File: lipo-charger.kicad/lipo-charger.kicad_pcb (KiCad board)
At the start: 2 copper layers, 23 x 35 mm, 20 parts, among them J1 JST-PH2 Device, J2 Alt Device, J3 JST-PH2 Bat, J4 Alt Bat, U1 MCP73831-2-OT, U2 XB6166IS

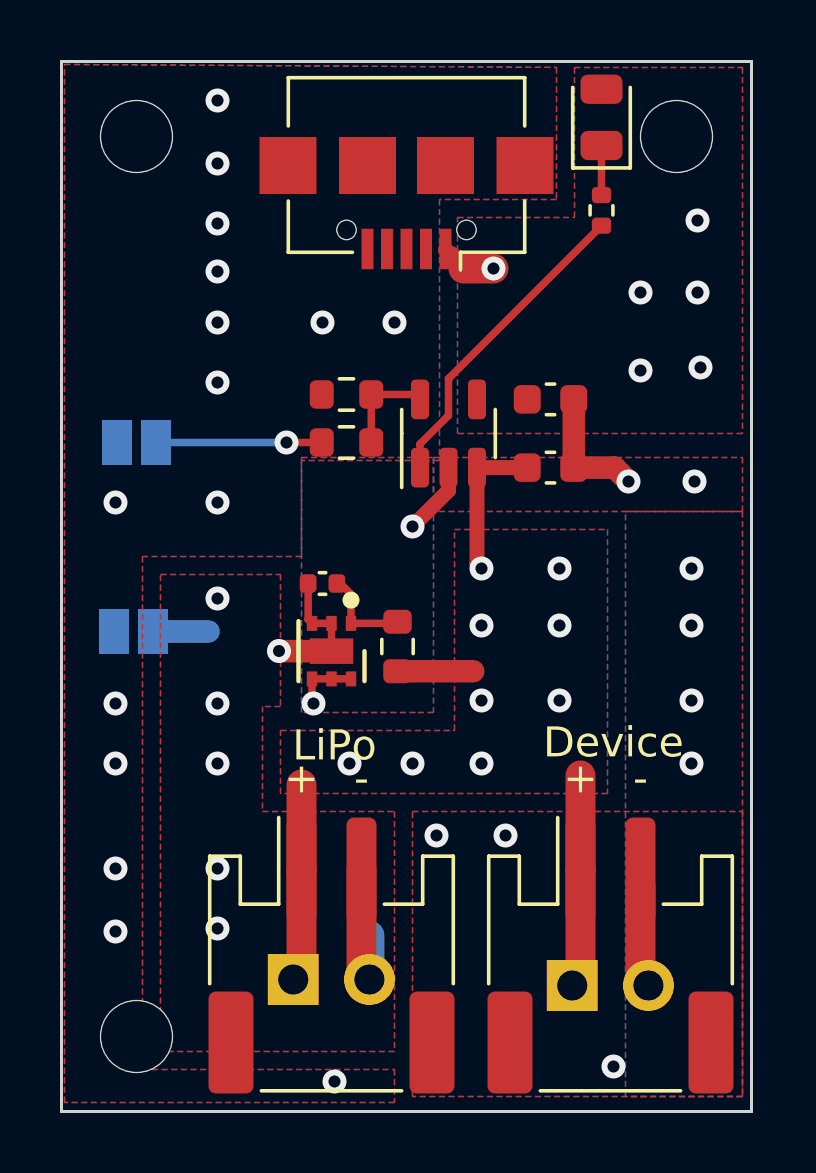
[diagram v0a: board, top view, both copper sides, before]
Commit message: Rev 0.91: remove alternative connectors for LiPo and device
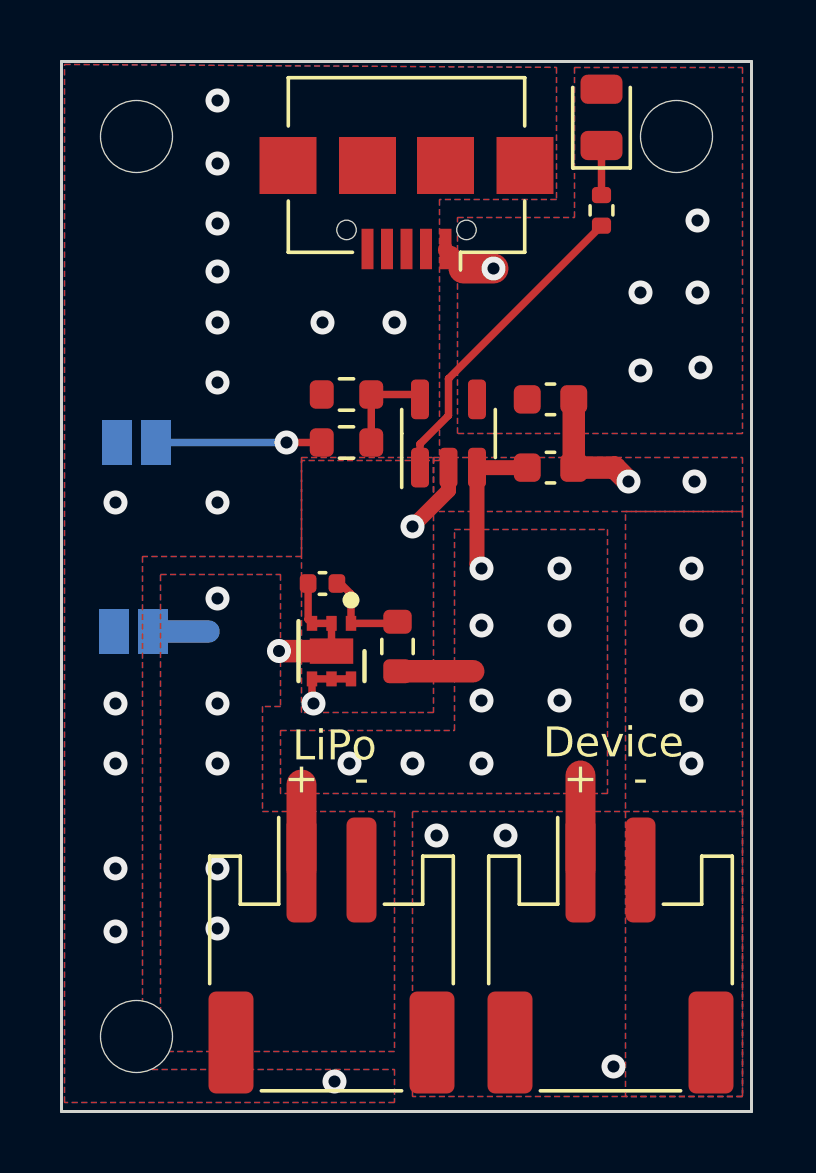
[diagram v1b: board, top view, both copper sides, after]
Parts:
- removed J2: Alt Device, Connector_PinHeader_2.54mm:PinHeader_1x02_P2.54mm_Vertical
- removed J4: Alt Bat, Connector_PinHeader_2.54mm:PinHeader_1x02_P2.54mm_Vertical
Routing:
- net +BATT: track 21.4 -> 13.6 mm
- net -BATT: track 11.8 -> 6.56 mm
- net GND: track 12.7 -> 9.27 mm
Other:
- board text added: "https://github.com/bablokb/ pcb-lipo-charger Rev: 0.91"
- board text removed: "https://github.com/bablokb/ pcb-lipo-charger Rev: 0.9"
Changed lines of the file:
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@@
     (pad "" np_thru_hole circle (at 0 0) (size 2.4 2.4) (drill 2.4) (layers F&B.Cu *.Mask))
-  )
-  (footprint "Connector_PinHeader_2.54mm:PinHeader_1x02_P2.54mm_Vertical" (layer "B.Cu")
-    (at 117.025 130.8 -90)
-    (descr "Through hole straight pin header, 1x02, 2.54mm pitch, single row")
-    (tags "Through hole pin header THT 1x02 2.54mm single row")
-    (property "Sheetfile" "lipo-charger.kicad_sch")
-    (property "Sheetname" "")
-    (property "exclude_from_bom" "")
-    (attr through_hole exclude_from_bom)
-    (fp_text reference "J2" (at -2.1 -1.275 180) (layer "B.SilkS") hide
-      (effects (font (size 1 1) (thickness 0.15)) (justify mirror))
-    )
-    (fp_text value "Alt Device" (at 0 -4.87 90) (layer "B.Fab") hide
-      (effects (font (size 1 1) (thickness 0.15)) (justify mirror))
-    )
-    (fp_text user "${REFERENCE}" (at 0 -1.27) (layer "B.Fab")
-      (effects (font (size 1 1) (thickness 0.15)) (justify mirror))
-    )
-    (fp_line (start 1.33 -1.27) (end 1.33 -3.87) (layer "B.SilkS") (width 0.12))
-    (fp_line (start -1.33 1.33) (end 0 1.33) (layer "B.SilkS") (width 0.12))
-    (fp_line (start -1.33 -1.27) (end 1.33 -1.27) (layer "B.SilkS") (width 0.12))
-    (fp_line (start -1.33 -3.87) (end 1.33 -3.87) (layer "B.SilkS") (width 0.12))
-    (fp_line (start -1.33 -1.27) (end -1.33 -3.87) (layer "B.SilkS") (width 0.12))
-    (fp_line (start -1.33 0) (end -1.33 1.33) (layer "B.SilkS") (width 0.12))
-    (fp_line (start -1.8 -4.35) (end 1.8 -4.35) (layer "B.CrtYd") (width 0.05))
-    (fp_line (start 1.8 1.8) (end -1.8 1.8) (layer "B.CrtYd") (width 0.05))
-    (fp_line (start -1.8 1.8) (end -1.8 -4.35) (layer "B.CrtYd") (width 0.05))
-    (fp_line (start 1.8 -4.35) (end 1.8 1.8) (layer "B.CrtYd") (width 0.05))
-    (fp_line (start 1.27 1.27) (end 1.27 -3.81) (layer "B.Fab") (width 0.1))
-    (fp_line (start -0.635 1.27) (end 1.27 1.27) (layer "B.Fab") (width 0.1))
-    (fp_line (start -1.27 -3.81) (end -1.27 0.635) (layer "B.Fab") (width 0.1))
-    (fp_line (start -1.27 0.635) (end -0.635 1.27) (layer "B.Fab") (width 0.1))
-    (fp_line (start 1.27 -3.81) (end -1.27 -3.81) (layer "B.Fab") (width 0.1))
-    (pad "1" thru_hole rect (at 0 0 270) (size 1.7 1.7) (drill 1) (layers *.Cu *.Mask)
-      (net 3 "+BATT") (pinfunction "Pin_1") (pintype "passive"))
-    (pad "2" thru_hole oval (at 0 -2.54 270) (size 1.7 1.7) (drill 1) (layers *.Cu *.Mask)
-      (net 2 "GND") (pinfunction "Pin_2") (pintype "passive"))
-    (model "${KICAD6_3DMODEL_DIR}/Connector_PinHeader_2.54mm.3dshapes/PinHeader_1x02_P2.54mm_Vertical.wrl"
-      (offset (xyz 0 0 0))
-      (scale (xyz 1 1 1))
-      (rotate (xyz 0 0 0))
-    )
-  )
-  (footprint "Connector_PinHeader_2.54mm:PinHeader_1x02_P2.54mm_Vertical" (layer "B.Cu")
-    (at 107.725 130.6 -90)
-    (descr "Through hole straight pin header, 1x02, 2.54mm pitch, single row")
-    (tags "Through hole pin header THT 1x02 2.54mm single row")
-    (property "Sheetfile" "lipo-charger.kicad_sch")
-    (property "Sheetname" "")
-    (property "exclude_from_bom" "")
-    (attr through_hole exclude_from_bom)
-    (fp_text reference "J4" (at -2.05 -1.125 180) (layer "B.SilkS") hide
-      (effects (font (size 1 1) (thickness 0.15)) (justify mirror))
-    )
-    (fp_text value "Alt Bat" (at 0 -4.87 90) (layer "B.Fab") hide
-      (effects (font (size 1 1) (thickness 0.15)) (justify mirror))
-    )
-    (fp_text user "${REFERENCE}" (at 0 -1.27) (layer "B.Fab")
-      (effects (font (size 1 1) (thickness 0.15)) (justify mirror))
-    )
-    (fp_line (start -1.33 1.33) (end 0 1.33) (layer "B.SilkS") (width 0.12))
-    (fp_line (start 1.33 -1.27) (end 1.33 -3.87) (layer "B.SilkS") (width 0.12))
-    (fp_line (start -1.33 -3.87) (end 1.33 -3.87) (layer "B.SilkS") (width 0.12))
-    (fp_line (start -1.33 0) (end -1.33 1.33) (layer "B.SilkS") (width 0.12))
-    (fp_line (start -1.33 -1.27) (end -1.33 -3.87) (layer "B.SilkS") (width 0.12))
-    (fp_line (start -1.33 -1.27) (end 1.33 -1.27) (layer "B.SilkS") (width 0.12))
-    (fp_line (start 1.8 -4.35) (end 1.8 1.8) (layer "B.CrtYd") (width 0.05))
-    (fp_line (start 1.8 1.8) (end -1.8 1.8) (layer "B.CrtYd") (width 0.05))
-    (fp_line (start -1.8 1.8) (end -1.8 -4.35) (layer "B.CrtYd") (width 0.05))
-    (fp_line (start -1.8 -4.35) (end 1.8 -4.35) (layer "B.CrtYd") (width 0.05))
-    (fp_line (start -0.635 1.27) (end 1.27 1.27) (layer "B.Fab") (width 0.1))
-    (fp_line (start 1.27 -3.81) (end -1.27 -3.81) (layer "B.Fab") (width 0.1))
-    (fp_line (start -1.27 0.635) (end -0.635 1.27) (layer "B.Fab") (width 0.1))
-    (fp_line (start -1.27 -3.81) (end -1.27 0.635) (layer "B.Fab") (width 0.1))
-    (fp_line (start 1.27 1.27) (end 1.27 -3.81) (layer "B.Fab") (width 0.1))
-    (pad "1" thru_hole rect (at 0 0 270) (size 1.7 1.7) (drill 1) (layers *.Cu *.Mask)
-      (net 3 "+BATT") (pinfunction "Pin_1") (pintype "passive"))
-    (pad "2" thru_hole oval (at 0 -2.54 270) (size 1.7 1.7) (drill 1) (layers *.Cu *.Mask)
-      (net 5 "-BATT") (pinfunction "Pin_2") (pintype "passive"))
-    (model "${KICAD6_3DMODEL_DIR}/Connector_PinHeader_2.54mm.3dshapes/PinHeader_1x02_P2.54mm_Vertical.wrl"
-      (offset (xyz 0 0 0))
-      (scale (xyz 1 1 1))
-      (rotate (xyz 0 0 0))
-    )
   )
   (footprint "Jumper:SolderJumper-2_P1.3mm_Open_Pad1.0x1.5mm" (layer "B.Cu")
@@
   (gr_line (start 100 135) (end 100 100) (layer "Edge.Cuts") (width 0.1))
   (gr_line (start 123 135) (end 100 135) (layer "Edge.Cuts") (width 0.1))
-  (gr_text "https://github.com/bablokb/\n  pcb-lipo-charger\nRev: 0.9" (at 121.8 106.2) (layer "B.SilkS")
+  (gr_text "https://github.com/bablokb/\n  pcb-lipo-charger\nRev: 0.91" (at 121.8 106.2) (layer "B.SilkS")
     (effects (font (size 0.9 0.9) (thickness 0.15)) (justify left mirror))
-  )
-  (gr_text "Device" (at 118.3 126.8) (layer "B.SilkS")
-    (effects (font (size 1 1) (thickness 0.15)) (justify mirror))
-  )
-  (gr_text "-" (at 110.3 128.6 180) (layer "B.SilkS")
-    (effects (font (size 1 1) (thickness 0.15)) (justify mirror))
   )
   (gr_text "No\nProtect" (at 102.4 120.3 270) (layer "B.SilkS")
@@
     (effects (font (size 1 1) (thickness 0.15)) (justify left mirror))
   )
-  (gr_text "+" (at 107.7 128.6 180) (layer "B.SilkS")
-    (effects (font (size 1 1) (thickness 0.15)) (justify mirror))
-  )
-  (gr_text "LiPo" (at 109 126.9) (layer "B.SilkS")
-    (effects (font (size 1 1) (thickness 0.15)) (justify mirror))
-  )
-  (gr_text "-" (at 119.6 128.6 180) (layer "B.SilkS")
-    (effects (font (size 1 1) (thickness 0.15)) (justify mirror))
-  )
   (gr_text "I charge: 200mA\nI fast:    500mA\n\nI load: 900mA max" (at 121.7 118.2) (layer "B.SilkS")
     (effects (font (size 1 1) (thickness 0.15)) (justify left mirror))
-  )
-  (gr_text "+" (at 117 128.6 180) (layer "B.SilkS")
-    (effects (font (size 1 1) (thickness 0.15)) (justify mirror))
   )
   (gr_text "+" (at 108 123.9) (layer "F.SilkS")
@@
   (segment (start 117.075 113.5375) (end 118.4375 113.5375) (width 0.75) (layer "F.Cu") (net 2))
   (segment (start 112.9 114.3) (end 111.7 115.5) (width 0.5) (layer "F.Cu") (net 2))
-  (segment (start 119.565 130.8) (end 119.3 130.535) (width 1) (layer "F.Cu") (net 2))
   (segment (start 112.9 113.5375) (end 112.9 114.3) (width 0.5) (layer "F.Cu") (net 2))
   (segment (start 118.4375 113.5375) (end 118.9 114) (width 0.75) (layer "F.Cu") (net 2))
@@
   (segment (start 117.075 113.5375) (end 117.075 111.2625) (width 0.75) (layer "F.Cu") (net 2))
   (segment (start 109.65 120.579304) (end 108.35 120.579304) (width 0.25) (layer "F.Cu") (net 2))
-  (segment (start 119.3 130.535) (end 119.3 127.48) (width 1) (layer "F.Cu") (net 2))
   (via (at 105.2 101.3) (size 0.8) (drill 0.4) (layers "F.Cu" "B.Cu") (free) (net 2))
   (via (at 105.2 110.7) (size 0.8) (drill 0.4) (layers "F.Cu" "B.Cu") (free) (net 2))
@@
   (segment (start 113.85 113.5375) (end 115.525 113.5375) (width 0.5) (layer "F.Cu") (net 3))
   (segment (start 117.3 126.95) (end 117.3 123.8) (width 1) (layer "F.Cu") (net 3))
-  (segment (start 108 130.325) (end 107.725 130.6) (width 1) (layer "F.Cu") (net 3))
-  (segment (start 117.3 126.95) (end 117.3 130.525) (width 1) (layer "F.Cu") (net 3))
-  (segment (start 117.3 130.525) (end 117.025 130.8) (width 1) (layer "F.Cu") (net 3))
-  (segment (start 108 126.95) (end 108 130.325) (width 1) (layer "F.Cu") (net 3))
   (segment (start 108 126.95) (end 108 124.1) (width 1) (layer "F.Cu") (net 3))
   (segment (start 113.85 113.5375) (end 113.85 116.75) (width 0.5) (layer "F.Cu") (net 3))
@@
   (segment (start 109.65 118.729304) (end 111.145696 118.729304) (width 0.25) (layer "F.Cu") (net 4))
   (segment (start 109.18 117.4) (end 109.3 117.4) (width 0.25) (layer "F.Cu") (net 4))
-  (segment (start 110 130.335) (end 110 126.95) (width 1) (layer "F.Cu") (net 5))
   (segment (start 108.22 117.4) (end 108.22 118.599304) (width 0.25) (layer "F.Cu") (net 5))
-  (segment (start 110.265 130.6) (end 110 130.335) (width 1) (layer "F.Cu") (net 5))
   (segment (start 108.35 118.729304) (end 109 118.729304) (width 0.25) (layer "F.Cu") (net 5))
   (segment (start 108.22 118.599304) (end 108.35 118.729304) (width 0.25) (layer "F.Cu") (net 5))
@@
   (via (at 105.2 128.9) (size 0.8) (drill 0.4) (layers "F.Cu" "B.Cu") (free) (net 5))
   (segment (start 103.05 119) (end 104.9 119) (width 0.75) (layer "B.Cu") (net 5))
-  (segment (start 110.265 130.6) (end 110.265 129.135) (width 1) (layer "B.Cu") (net 5))
   (segment (start 118 104.4525) (end 118 102.8) (width 0.25) (layer "F.Cu") (net 6))
   (segment (start 108.675 112.7) (end 107.5 112.7) (width 0.25) (layer "F.Cu") (net 7))
